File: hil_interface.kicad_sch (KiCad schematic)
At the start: 0 parts

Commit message: Update schematic for DebugBoard with connector and power symbols.
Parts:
- added J1001: Conn_02x10_Odd_Even, symbol Connector_Generic:Conn_02x10_Odd_Even
- added J203: Conn_02x10_Row_Letter_First, PRJ:PCN10-20P-2.54DS, symbol Connector_Generic:Conn_02x10_Row_Letter_First
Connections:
- new net ADC_IN0: J1001.16 (Pin_16)
- new net ADC_IN1: J1001.18 (Pin_18)
- new net BOOT0: J1001.4 (Pin_4)
- new net DAC_OUT: J1001.20 (Pin_20)
- new net GND: J1001.12 (Pin_12), J1001.15 (Pin_15), J1001.17 (Pin_17), J1001.19 (Pin_19), J1001.2 (Pin_2), J1001.7 (Pin_7), J203.a1 (Pin_a1), J203.a8 (Pin_a8), J203.b1 (Pin_b1), J203.b8 (Pin_b8)
- new net I2C_SCK: J1001.14 (Pin_14)
- new net I2C_SDA: J1001.13 (Pin_13)
- new net RESET: J1001.3 (Pin_3)
- new net SWCLK: J1001.6 (Pin_6)
- new net SWDIO: J1001.5 (Pin_5)
- new net UART0_RX: J1001.8 (Pin_8)
- new net UART0_TX: J1001.9 (Pin_9)
- new net UART1_RX: J1001.10 (Pin_10)
- new net UART1_TX: J1001.11 (Pin_11)
- new net USB+: J203.a5 (Pin_a5)
- new net USB-: J203.b5 (Pin_b5)
- new net VCC: J203.a6 (Pin_a6), J203.a7 (Pin_a7), J203.b6 (Pin_b6), J203.b7 (Pin_b7)
- new net VCC_3V3: J1001.1 (Pin_1)
- no-connect marks 0 -> 10
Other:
- added sheet SW Port (sw_port.kicad_sch)

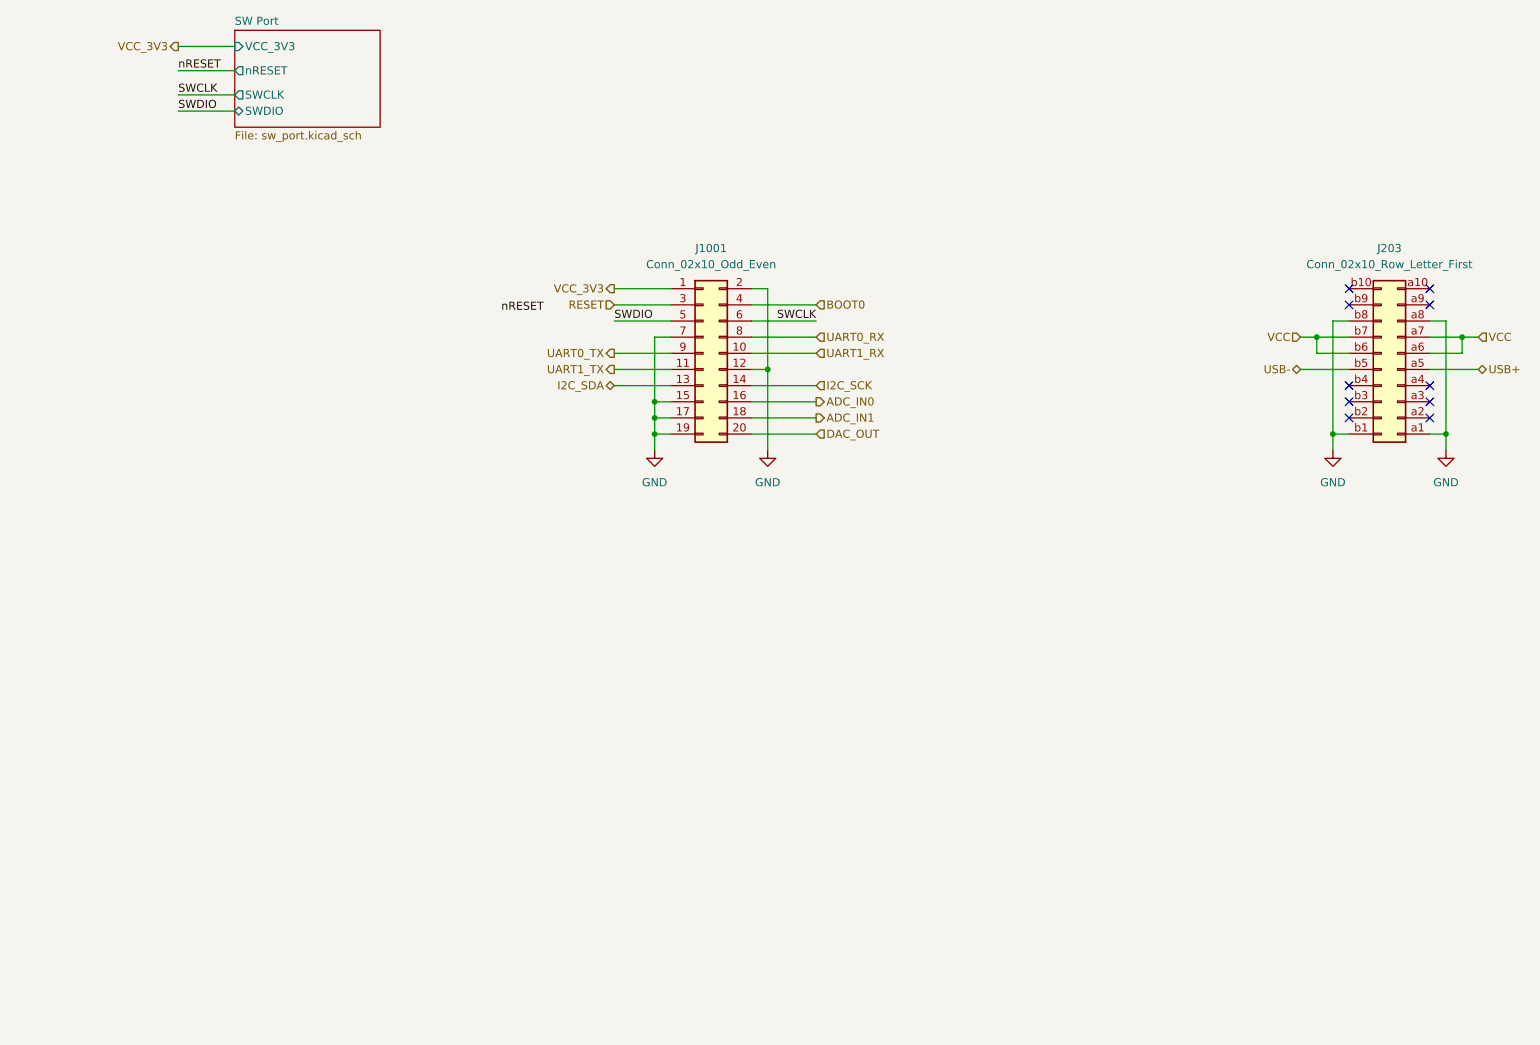
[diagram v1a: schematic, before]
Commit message: Update USB-C and USB-Hub Schematics with New Titles and Reference Changes
- Changed title from "DebugBoard" to "USB-C" in usb_c.kicad_sch.
- Changed title from "DebugBoard" to "USB-Hub" in usb_hub.kicad_sch.
- Updated multiple component references in usb_c.kicad_sch to new identifiers (#PWR0301 to #PWR0312, D301, U301, etc.).
- Updated component reference from "R103" to "R501" in usb_hub.kicad_sch.
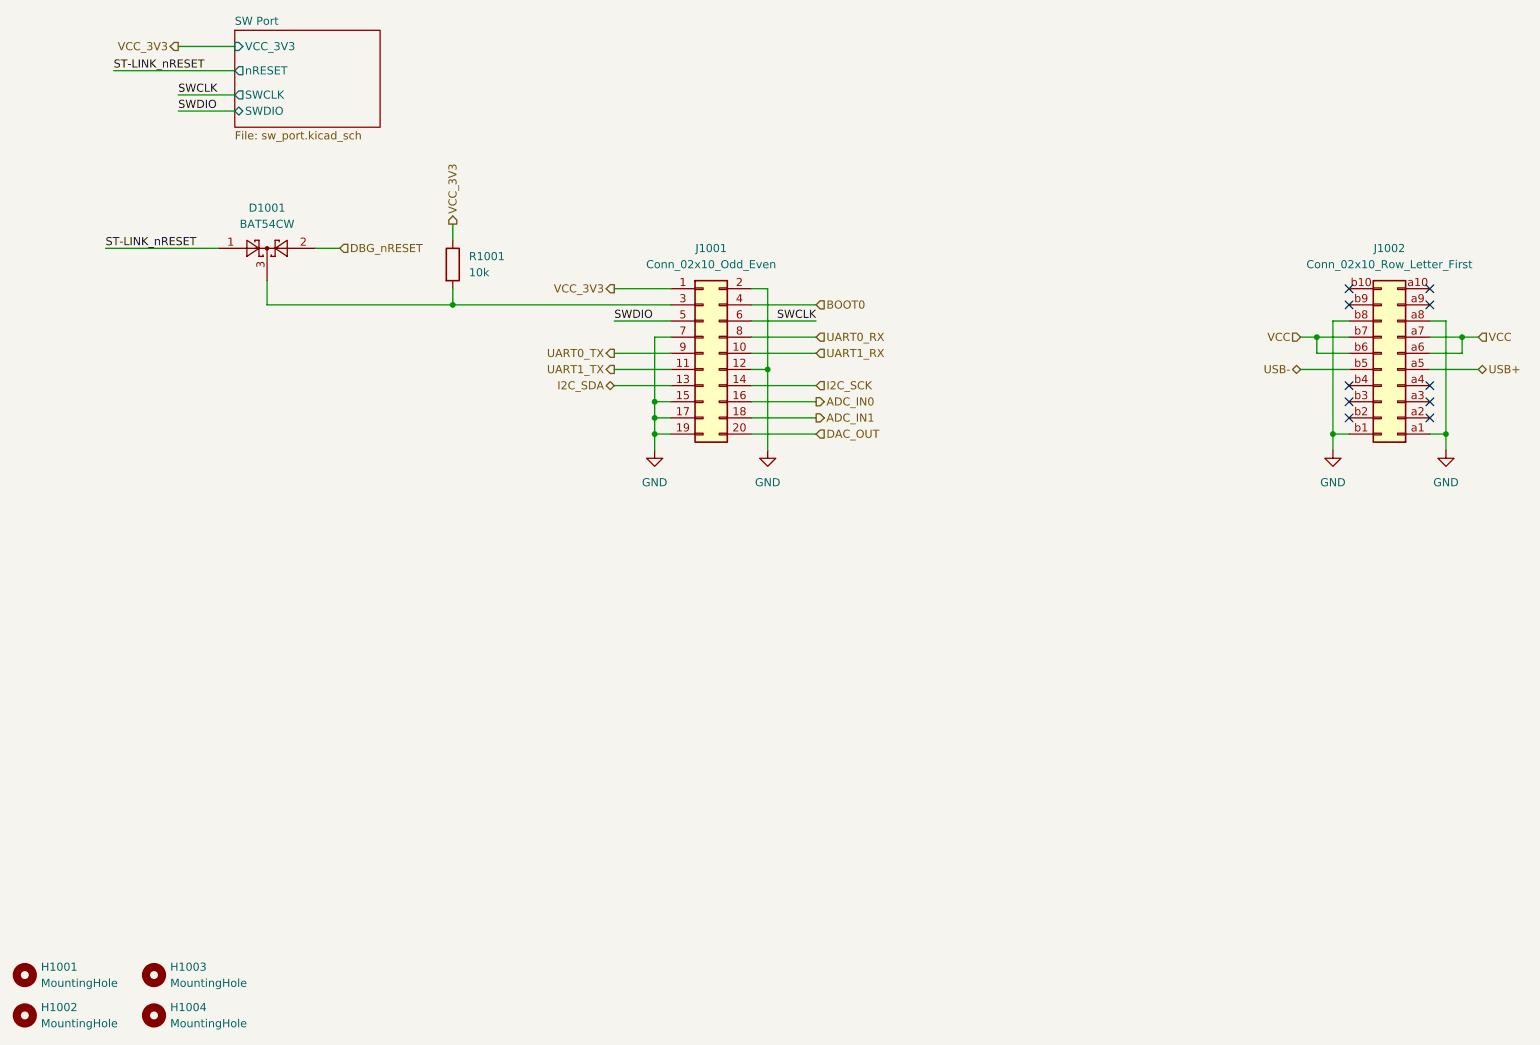
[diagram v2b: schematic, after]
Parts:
- added D1001: BAT54CW, Package_TO_SOT_SMD:SOT-323_SC-70, symbol Diode:BAT54CW
- added H1001, H1002, H1003, H1004: MountingHole, MountingHole:MountingHole_3.2mm_M3, symbol Mechanical:MountingHole
- added R1001: 10k, Resistor_SMD:R_0805_2012Metric, symbol Device:R
- renumbered J203 to J1002
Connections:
- net VCC_3V3: now also R1001.1
- net RESET: no longer names the net of J1001.3 (Pin_3)
- net RESET: now also D1001.3, R1001.2
- new net DBG_nRESET: D1001.2
- new net ST-LINK_nRESET: D1001.1
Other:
- title: DebugBoard -> DUT Interface Header

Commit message: update pcb
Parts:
- removed H1001, H1002, H1003, H1004: MountingHole, MountingHole:MountingHole_3.2mm_M3, symbol Mechanical:MountingHole
- J1001: footprint (none) -> Connector_PinHeader_1.27mm:PinHeader_2x10_P1.27mm_Vertical
